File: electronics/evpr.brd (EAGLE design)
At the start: 97.2 x 41.3 mm, 117 parts, among them J1 10118193-0001LF, J2 B4P-VH(LF)(SN), Q1 AOD4184A, Q2 AOD4184A, T1 MMBT2222A, T2 MMBT2222A, T3 MMBT2222A, T5 MMBT2222A, U1 MC14044BDR2G, U2 BQ2057TTS, U3 ESP32-WROOM-32D, U5 AP2112K-3.3TRG1, U6 SN74AHCT125DR, U7 TPSM84824MOLR, U8 LTC4353CMSPBFMSOP-16_MS-M, X1 B3P-VH(LF)(SN), X2 B3P-VH(LF)(SN), X3 B3P-VH(LF)(SN)

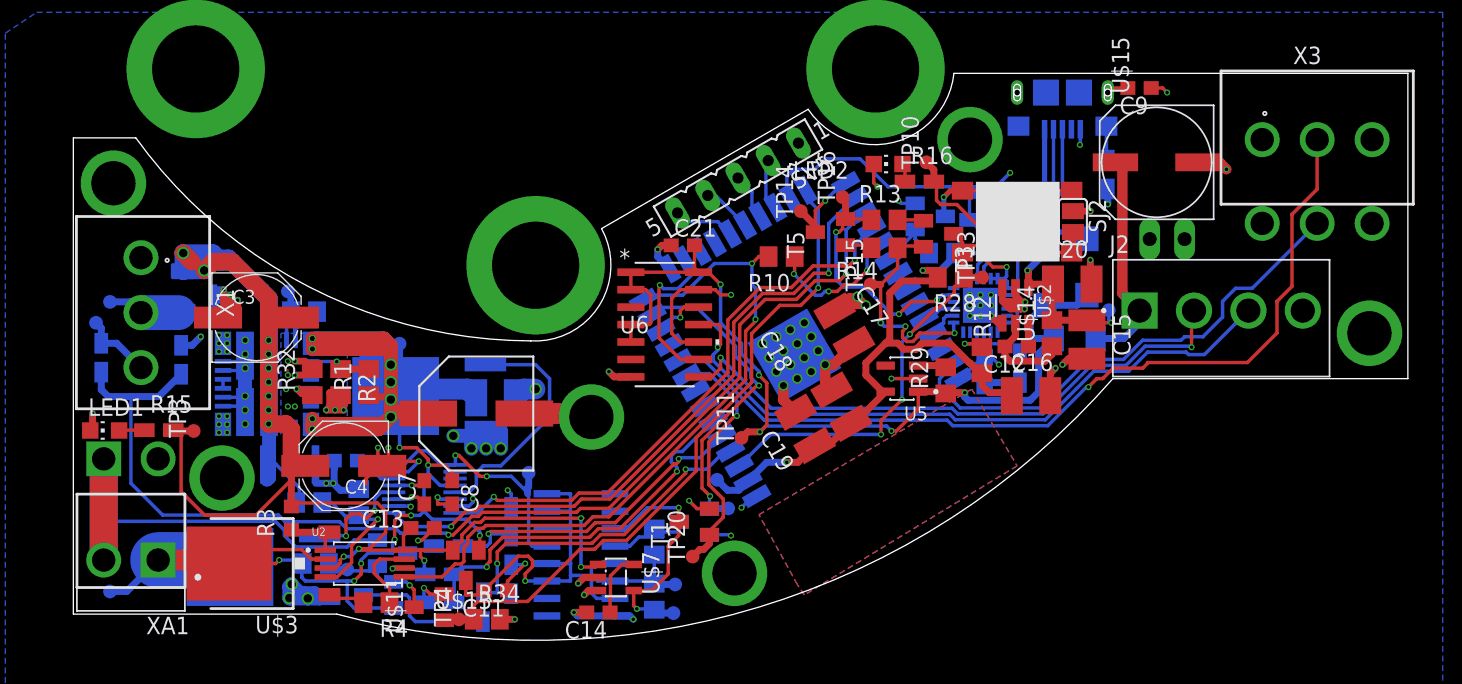
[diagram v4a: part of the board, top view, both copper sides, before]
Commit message: Sprinkled about some groundplane vias
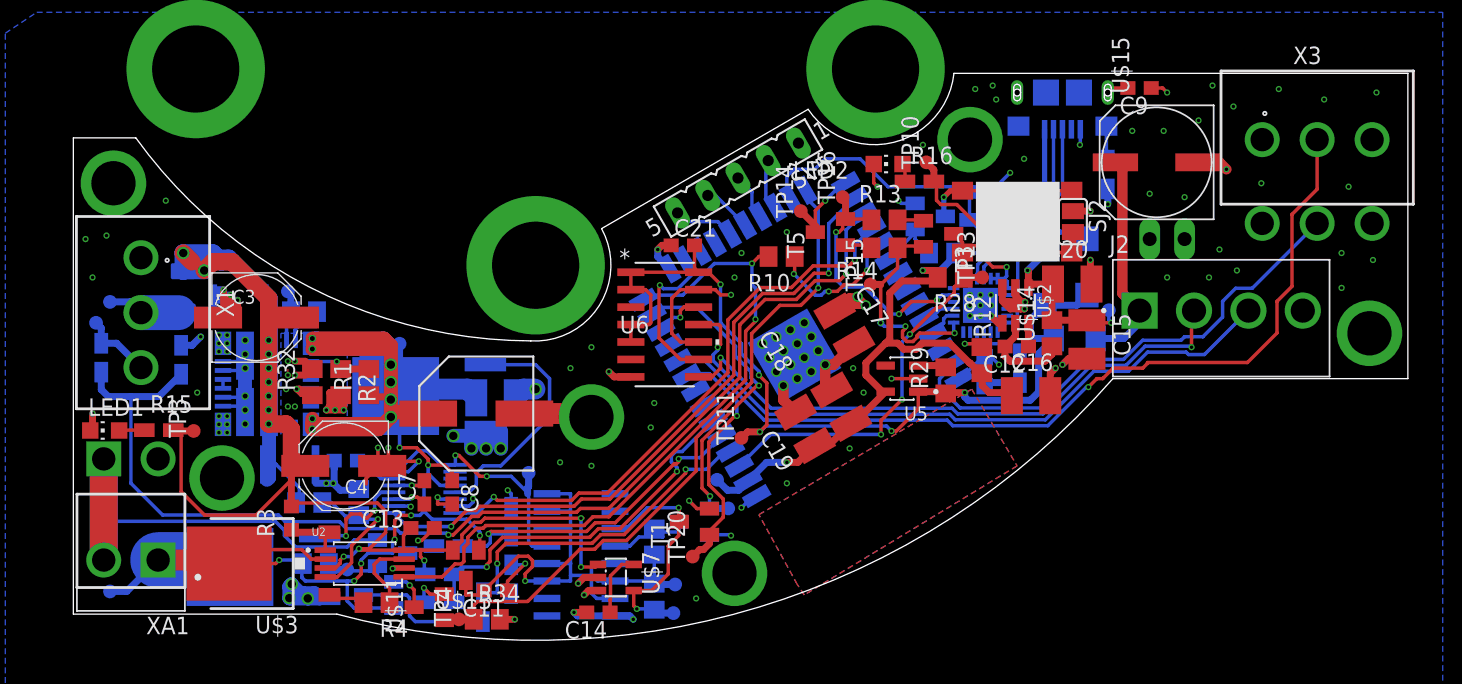
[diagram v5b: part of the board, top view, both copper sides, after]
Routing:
- net GND: vias 89 -> 132
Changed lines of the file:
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@@
 <layer number="20" name="Dimension" color="24" fill="1" visible="yes" active="yes"/>
 <layer number="21" name="tPlace" color="7" fill="1" visible="yes" active="yes"/>
-<layer number="22" name="bPlace" color="7" fill="1" visible="no" active="yes"/>
+<layer number="22" name="bPlace" color="7" fill="1" visible="yes" active="yes"/>
 <layer number="23" name="tOrigins" color="15" fill="1" visible="yes" active="yes"/>
-<layer number="24" name="bOrigins" color="15" fill="1" visible="no" active="yes"/>
+<layer number="24" name="bOrigins" color="15" fill="1" visible="yes" active="yes"/>
 <layer number="25" name="tNames" color="7" fill="1" visible="no" active="yes"/>
 <layer number="26" name="bNames" color="7" fill="1" visible="no" active="yes"/>
@@
 <layer number="37" name="tTest" color="7" fill="1" visible="no" active="yes"/>
 <layer number="38" name="bTest" color="7" fill="1" visible="no" active="yes"/>
-<layer number="39" name="tKeepout" color="4" fill="11" visible="yes" active="yes"/>
-<layer number="40" name="bKeepout" color="1" fill="11" visible="yes" active="yes"/>
+<layer number="39" name="tKeepout" color="4" fill="11" visible="no" active="yes"/>
+<layer number="40" name="bKeepout" color="1" fill="11" visible="no" active="yes"/>
 <layer number="41" name="tRestrict" color="4" fill="10" visible="no" active="yes"/>
 <layer number="42" name="bRestrict" color="1" fill="10" visible="no" active="yes"/>
@@
 <layer number="49" name="Reference" color="7" fill="1" visible="no" active="yes"/>
 <layer number="51" name="tDocu" color="7" fill="1" visible="yes" active="yes"/>
-<layer number="52" name="bDocu" color="7" fill="1" visible="no" active="yes"/>
+<layer number="52" name="bDocu" color="7" fill="1" visible="yes" active="yes"/>
 <layer number="88" name="SimResults" color="9" fill="1" visible="no" active="no"/>
 <layer number="89" name="SimProbes" color="9" fill="1" visible="no" active="no"/>
@@
 <vertex x="19.558" y="-52.578"/>
 </polygon>
+<via x="2.54" y="-36.068" extent="1-16" drill="0.254"/>
+<via x="8.636" y="-38.608" extent="1-16" drill="0.254"/>
+<via x="4.064" y="-43.18" extent="1-16" drill="0.254"/>
+<via x="1.778" y="-42.926" extent="1-16" drill="0.254"/>
+<via x="11.684" y="-52.832" extent="1-16" drill="0.254"/>
+<via x="18.288" y="-44.45" extent="1-16" drill="0.254"/>
+<via x="22.86" y="-41.91" extent="1-16" drill="0.254"/>
+<via x="23.114" y="-36.068" extent="1-16" drill="0.254"/>
+<via x="23.876" y="-37.846" extent="1-16" drill="0.254"/>
+<via x="14.478" y="-29.464" extent="1-16" drill="0.254"/>
+<via x="18.288" y="-26.162" extent="1-16" drill="0.254"/>
+<via x="14.986" y="-27.686" extent="1-16" drill="0.254"/>
+<via x="35.56" y="-20.828" extent="1-16" drill="0.254"/>
+<via x="33.528" y="-16.51" extent="1-16" drill="0.254"/>
+<via x="32.004" y="-15.748" extent="1-16" drill="0.254"/>
+<via x="33.274" y="-15.494" extent="1-16" drill="0.254"/>
+<via x="28.194" y="-19.812" extent="1-16" drill="0.254"/>
+<via x="43.434" y="-18.796" extent="1-16" drill="0.254"/>
+<via x="45.72" y="-18.796" extent="1-16" drill="0.254"/>
+<via x="44.704" y="-23.368" extent="1-16" drill="0.254"/>
+<via x="47.244" y="-23.622" extent="1-16" drill="0.254"/>
+<via x="48.26" y="-18.034" extent="1-16" drill="0.254"/>
+<via x="49.276" y="-15.494" extent="1-16" drill="0.254"/>
+<via x="50.8" y="-17.018" extent="1-16" drill="0.254"/>
+<via x="57.404" y="-16.51" extent="1-16" drill="0.254"/>
+<via x="54.102" y="-15.748" extent="1-16" drill="0.254"/>
+<via x="52.832" y="-22.606" extent="1-16" drill="0.254"/>
+<via x="59.182" y="-22.86" extent="1-16" drill="0.254"/>
+<via x="61.214" y="-16.002" extent="1-16" drill="0.254"/>
+<via x="60.96" y="-28.194" extent="1-16" drill="0.254"/>
+<via x="58.674" y="-27.686" extent="1-16" drill="0.254"/>
+<via x="58.674" y="-30.226" extent="1-16" drill="0.254"/>
+<via x="51.054" y="-28.956" extent="1-16" drill="0.254"/>
+<via x="49.022" y="-29.464" extent="1-16" drill="0.254"/>
+<via x="49.784" y="-27.432" extent="1-16" drill="0.254"/>
+<via x="45.974" y="-29.464" extent="1-16" drill="0.254"/>
+<via x="8.382" y="-40.386" extent="1-16" drill="0.254"/>
+<via x="4.064" y="-34.544" extent="1-16" drill="0.254"/>
+<via x="-24.638" y="-37.846" extent="1-16" drill="0.254"/>
+<via x="-32.258" y="-29.464" extent="1-16" drill="0.254"/>
+<via x="-32.766" y="-26.67" extent="1-16" drill="0.254"/>
+<via x="-31.242" y="-26.416" extent="1-16" drill="0.254"/>
+<via x="-26.924" y="-23.876" extent="1-16" drill="0.254"/>
 <wire x1="-16.002" y1="-44.45" x2="-16.02741875" y2="-43.66258125" width="0" layer="19" extent="16-16"/>
 </signal>

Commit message: Final  changes before prototype run
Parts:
- removed TP1: PTR1TP10R, testpad:TP10R
- removed U$6: 8A, mccloud:FUSC3216X130N
- added SJ1: (no value), jumper:SJ
- added U$16: (no value), mccloud:SOT23
- moved C5 10.9 mm to (-11.8, -31.9)
- moved TP5 6.06 mm to (-14.7, -30.6), turned to 0 degrees
- moved TP2 4.58 mm to (-27.7, -34.3)
- moved Q1 0.57 mm to (-7.24, -38.4), turned to 90 degrees
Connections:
- removed net VRAW_PF: TP1.TP, U$6.1, X1.2
- net GND: now also SJ1.1, U$16.3
- net N$30: now also SJ1.2
- net SYS_POWER: now also Q1.4, Q2.4; no longer Q1.3, Q2.3
- net TACH_RAW: now also U$16.2
- net VBAT: now also Q2.3; no longer Q2.4
- net VCONV: now also Q1.3; no longer Q1.4
- net VRAW: now also U$16.1, X1.2; no longer U$6.2
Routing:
- net VBAT: track 63.5 -> 94.8 mm, vias 7 -> 11
- net VCONV: track 106.7 -> 79.8 mm, vias 10 -> 9
- net VRAW: track 126.1 -> 138.4 mm
- net N$34: track 4.68 -> 15.7 mm
- net N$10: track 17.6 -> 8.41 mm, vias 0 -> 2
- net VRAW_PF: track 8.16 -> 0.00 mm
- net SYS_POWER: track 36.3 -> 41.9 mm, vias 13 -> 18
- net TACH_RAW: track 5.27 -> 9.47 mm
- net N$30: track 19.1 -> 22.0 mm
- net GND: track 119.7 -> 117.7 mm, vias 132 -> 134
- net AGND: track 11.2 -> 12.9 mm
- net N$4: track 8.19 -> 7.31 mm
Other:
- outline, holes or cut-outs redrawn

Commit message: Updated all part numbers, created BOM, created order recommendation
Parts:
- C10: value 270µF -> 220µF

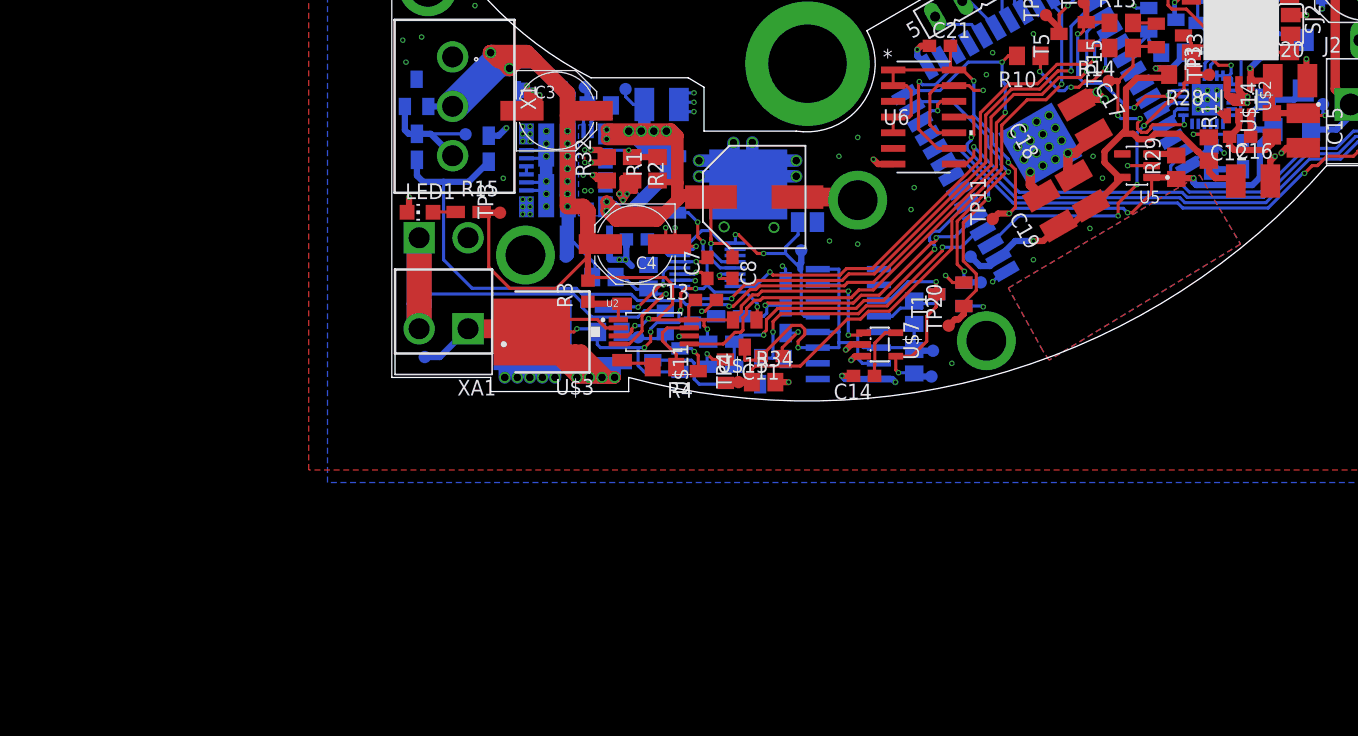
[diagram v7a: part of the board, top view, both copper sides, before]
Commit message: Update serial interface chip to only receive power from USB plug, utilize internal regulator instead of board 3.3V regulator. Also update bypass caps to be to spec. Also added .gitignore for electronics folder.
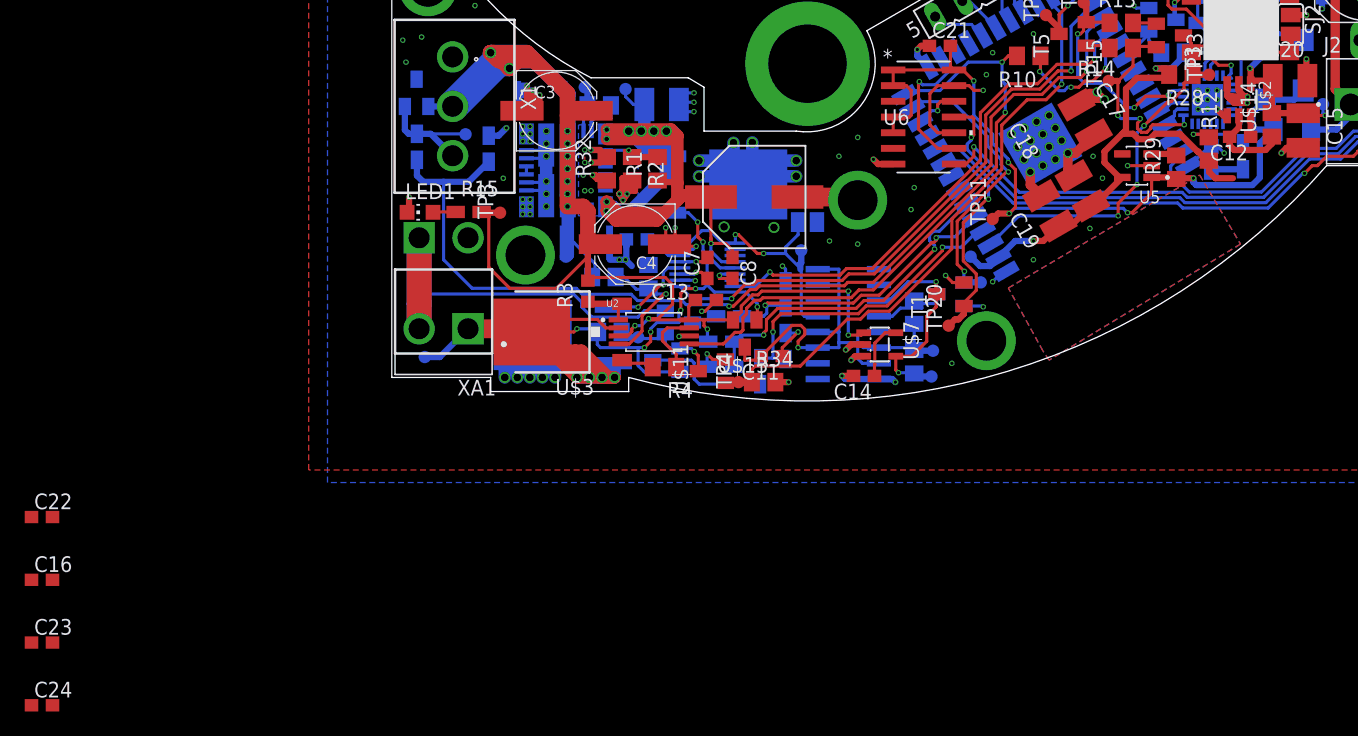
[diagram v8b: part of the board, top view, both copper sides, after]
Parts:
- added C22, C23: 0.1uF, eagle-ltspice:C0603
- added C24: 4.7uF, eagle-ltspice:C0603
- C16: value 10uF -> 4.7uF; device eagle-ltspice:C1210 -> eagle-ltspice:C0603
- moved C16 103.2 mm to (-62.0, -70.4)
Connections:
- removed net N$14: J1.1, R16.2, R18.2, TP10.TP, U$10.A
- new net N$39: R12.2, U$12.5
- new net N$40: C16.2, C22.2, U$12.6
- new net VUSB: C23.2, C24.2, J1.1, R16.2, R18.2, TP10.TP, U$10.A, U$12.7
- net 3.3V: no longer C16.1, R12.2, U$12.5, U$12.6, U$12.7
- net GND: now also C16.1, C22.1, C23.1, C24.1; no longer C16.2
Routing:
- net VUSB: track 0.00 -> 24.8 mm, vias 0 -> 3
- net N$14: track 24.8 -> 0.00 mm, vias 3 -> 0
- net GND: track 117.7 -> 115.5 mm, vias 134 -> 133
- net 3.3V: track 51.1 -> 49.2 mm
